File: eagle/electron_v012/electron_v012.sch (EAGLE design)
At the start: 92 parts, among them J1 SIM-NANO-4FF, J2 IPEX-20279-001E, U1 U-BLOX-SARA-U260, U2 SN74AVC4T245, U3 STM32F205RG, U4 MAX1704X, U5 SN74LVC1G07, U6 SN74LVC1G07, U8 SN74AVC4T245, X1 USB-MICROB, Y1 32Khz, Y2 26Mhz

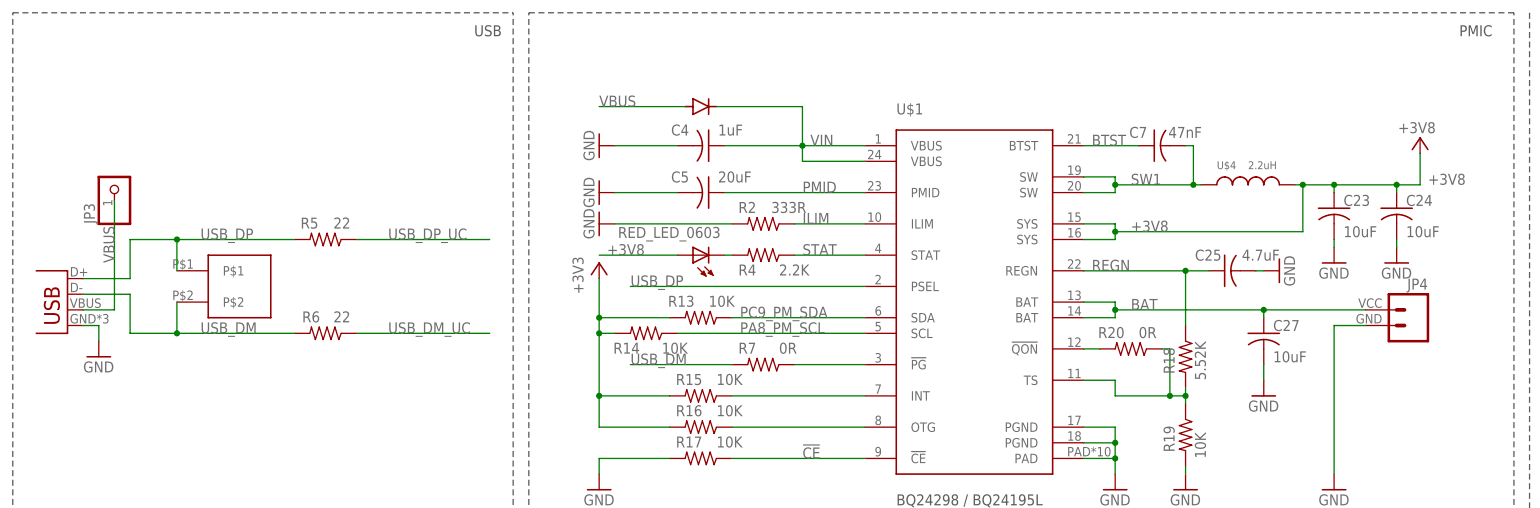
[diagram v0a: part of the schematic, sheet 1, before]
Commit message: added lipo and pmid 5v header
change log:
1. Exposed LiPo connection via a header
2. Exposed PMID boost 5V via a header
3. Lowered the 3V3 inductor and rotated its output cap to meet
datasheet recommendations
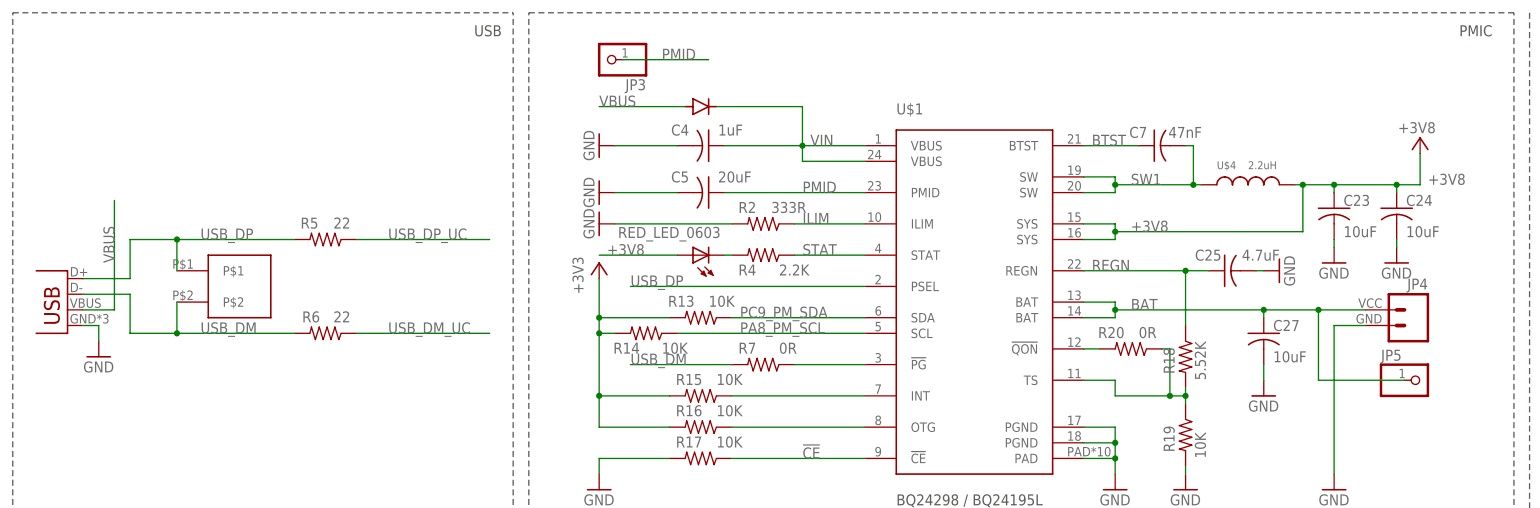
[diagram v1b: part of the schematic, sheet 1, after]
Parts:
- added JP5: (no value), Particle:PINHD-1X1NOSILK
- JP3: device Particle:PINHD-1X1 -> Particle:PINHD-1X1NOSILK
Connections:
- net BAT: now also JP5.1
- net PMID: now also JP3.1
- net VBUS: no longer JP3.1
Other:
- moved on the sheet: JP3
